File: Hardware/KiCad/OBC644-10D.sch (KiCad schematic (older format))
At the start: 57 parts, among them J1 CONN_11, J2 CONN_11, J3 CONN_4, J4 CONN_6, J5 53047, U1 LT1761ES5-3.3, U10 LT1761ES5-xx, U11 LT1761ES5-xx, U12 M25XX_ROM2, U2 ATMEGA644PA-AUR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

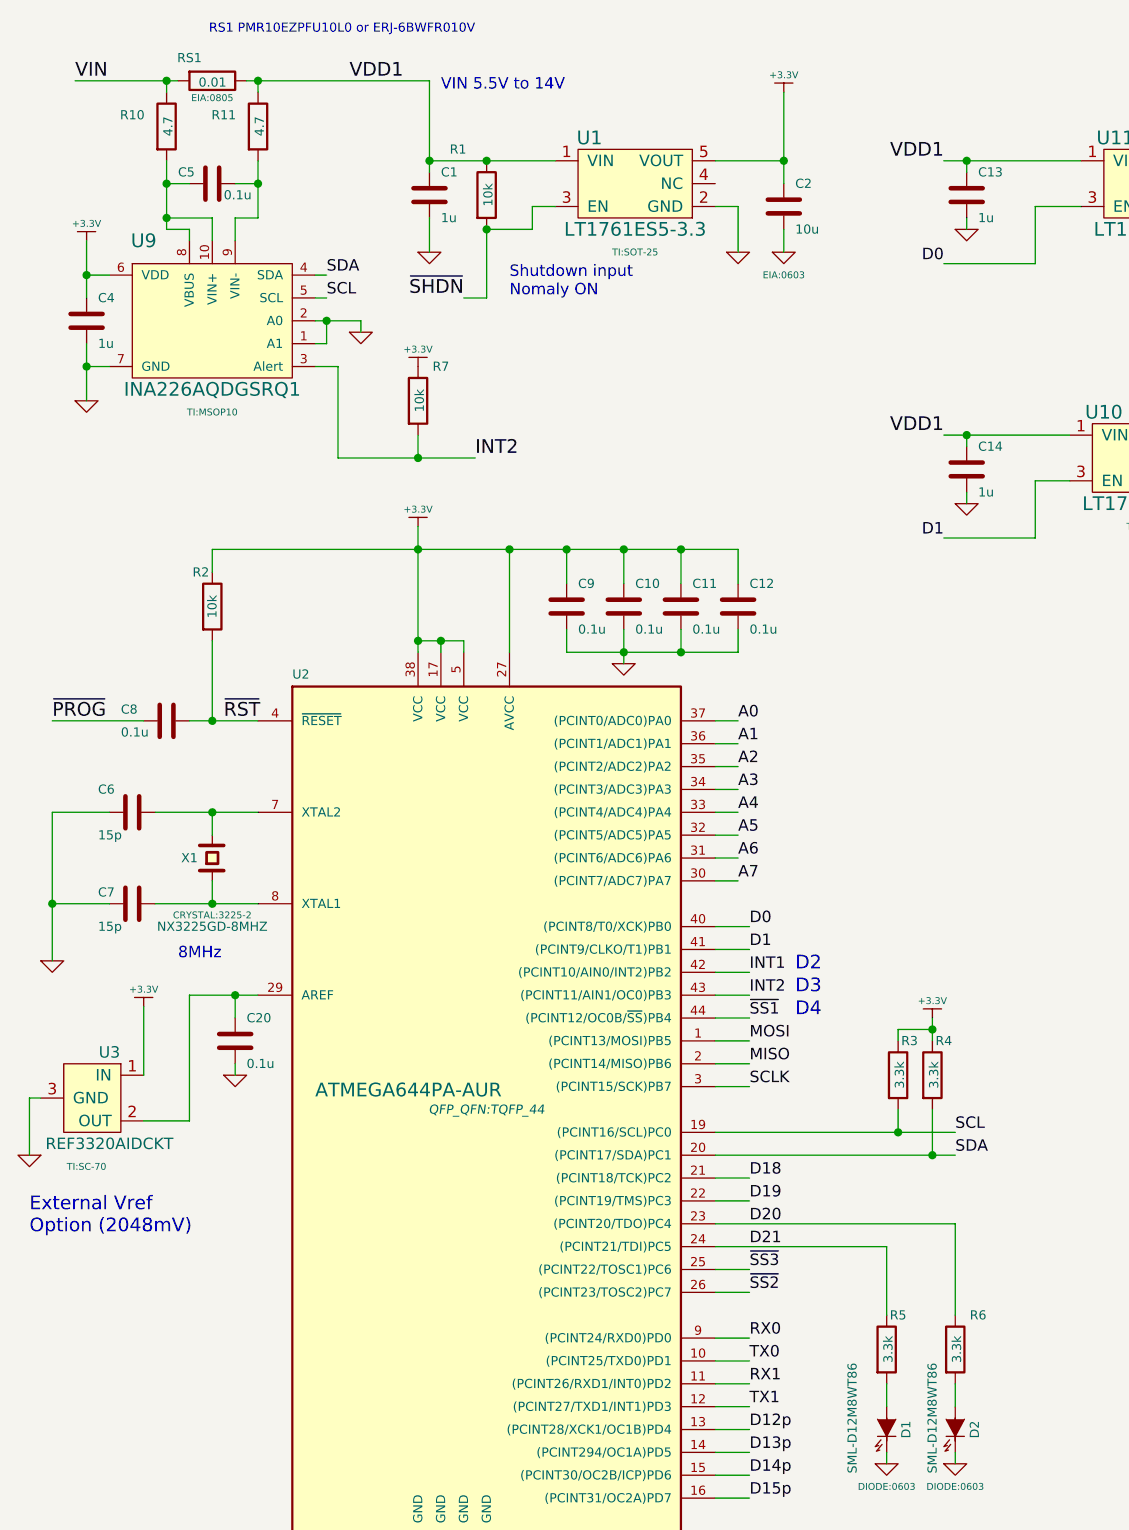
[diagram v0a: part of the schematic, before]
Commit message: Fix PCB and schematic
fix ShuntResistor size & routing
change R5,R6 value
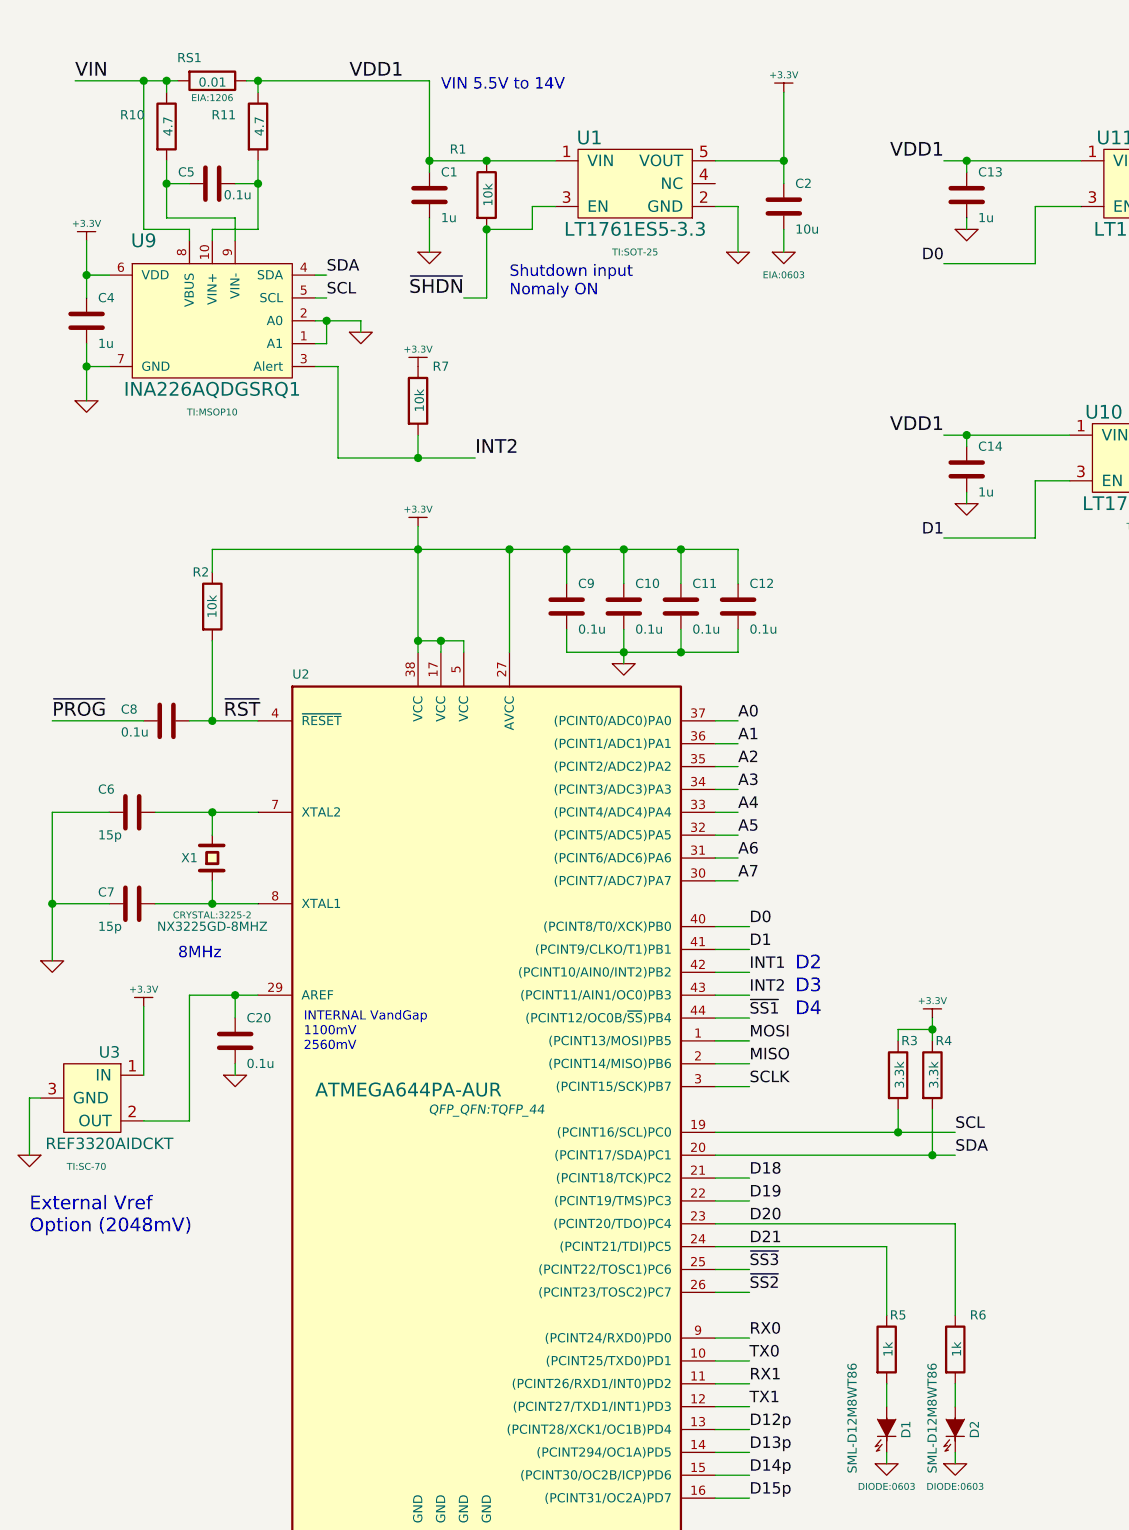
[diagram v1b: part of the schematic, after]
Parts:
- R5, R6: value 3.3k -> 1k
- RS1: footprint EIA:0805 -> EIA:1206
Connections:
- net VIN: now also U9.8 (VBUS)
- net at C5.2, R10.2: now also U9.9 (VIN-); no longer U9.10 (VIN+), U9.8 (VBUS)
- net at C5.1, R11.2: now also U9.10 (VIN+); no longer U9.9 (VIN-)
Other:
- note added: "INTERNAL VandGap\n1100mV\n2560mV"
- note removed: "RS1 PMR10EZPFU10L0 or ERJ-6BWFR010V"
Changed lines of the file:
@@
 LIBS:Sensor
 LIBS:socket
-LIBS:nLog_10DOF-cache
+LIBS:OBC644-10D-cache
 EELAYER 25 0
 EELAYER END
@@
 Sheet 1 1
 Title "OBC1284-10D"
-Date "2017-05-10"
-Rev "C"
+Date "2017-06-03"
+Rev "D"
 Comp "Kent Nakazawa (kent_n@outlook.com) (https://github.com/kentN)"
 Comment1 ""
@@
 P 4750 6300
 F 0 "R6" H 4850 6450 40  0000 C CNN
-F 1 "3.3k" V 4757 6301 40  0000 C CNN
+F 1 "1k" V 4757 6301 40  0000 C CNN
 F 2 "EIA:0402" V 4680 6300 30  0001 C CNN
 F 3 "" H 4750 6300 30  0000 C CNN
@@
 P 4450 6300
 F 0 "R5" H 4500 6450 40  0000 C CNN
-F 1 "3.3k" V 4457 6301 40  0000 C CNN
+F 1 "1k" V 4457 6301 40  0000 C CNN
 F 2 "EIA:0402" V 4380 6300 30  0001 C CNN
 F 3 "" H 4450 6300 30  0000 C CNN
@@
 F 0 "RS1" V 1400 650 40  0000 C CNN
 F 1 "0.01" V 1507 751 40  0000 C CNN
-F 2 "EIA:0805" V 1575 750 30  0000 C CNN
+F 2 "EIA:1206" V 1575 750 30  0000 C CNN
 F 3 "" H 1500 750 30  0000 C CNN
 	1    1500 750
@@
 Wire Wire Line
 	1400 5300 1200 5300
-Wire Wire Line
-	1600 1450 1600 1350
-Wire Wire Line
-	1600 1350 1700 1350
 Connection ~ 1700 750
-Wire Wire Line
-	1300 1350 1500 1350
-Wire Wire Line
-	1500 1350 1500 1450
 Connection ~ 1300 750
 Wire Wire Line
 	1400 1450 1400 1400
-Wire Wire Line
-	1400 1400 1300 1400
-Connection ~ 1300 1350
 Wire Wire Line
 	1050 1600 950  1600
@@
 	1700 750  1700 800
 Wire Wire Line
-	1300 1400 1300 1100
-Wire Wire Line
-	1700 1350 1700 1100
+	1700 1100 1700 1400
 Wire Wire Line
 	1600 1200 1700 1200
@@
 Text Notes 8300 1050 0    60   ~ 0
 Optional SMD ROMs
-Text Notes 2650 550  2    40   ~ 0
-RS1 PMR10EZPFU10L0 or ERJ-6BWFR010V
+Wire Wire Line
+	1300 1350 1300 1100
+Wire Wire Line
+	1400 1400 1200 1400
+Wire Wire Line
+	1200 1400 1200 750
+Connection ~ 1200 750
+Wire Wire Line
+	1300 1350 1600 1350
+Wire Wire Line
+	1600 1350 1600 1450
+Wire Wire Line
+	1700 1400 1500 1400
+Wire Wire Line
+	1500 1400 1500 1450
+Text Notes 1900 5000 0    40   ~ 0
+INTERNAL VandGap\n1100mV\n2560mV
 $EndSCHEMATC

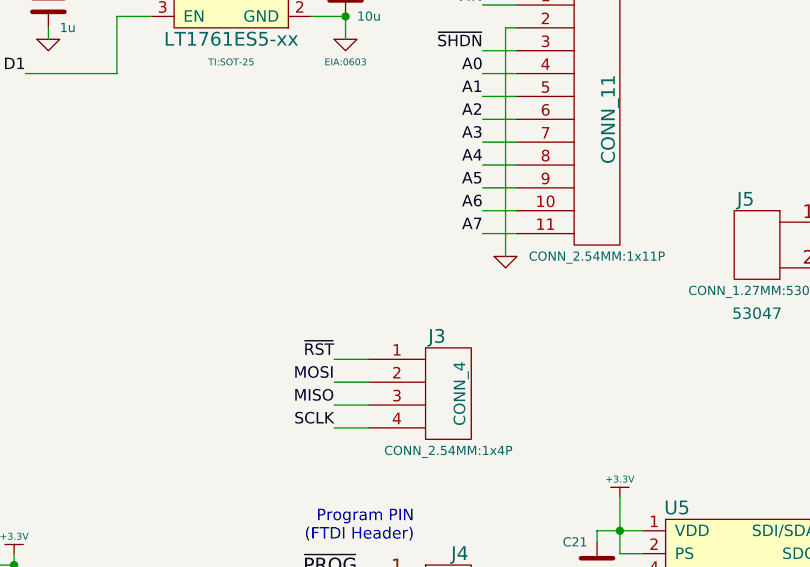
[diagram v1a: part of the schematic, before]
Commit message: Add VCPU OUTPUT
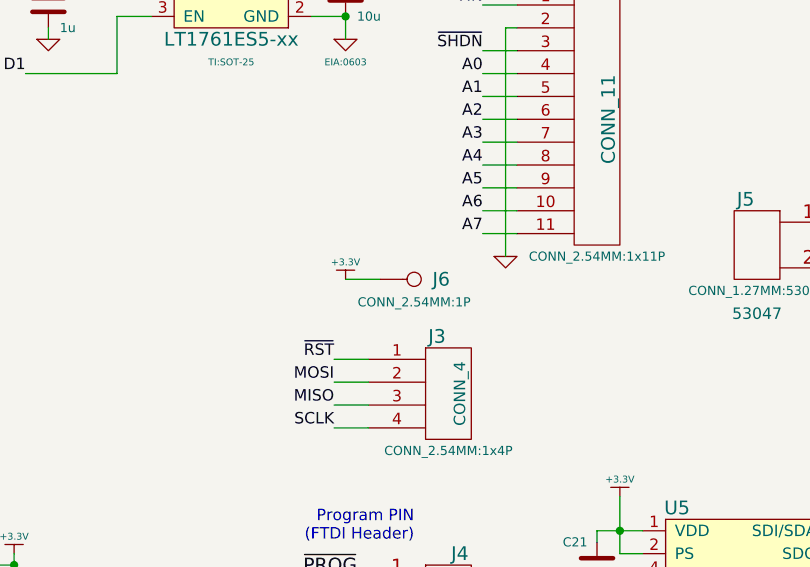
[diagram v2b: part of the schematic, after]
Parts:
- added J6: CONN_1, CONN_2.54MM:1P, symbol CONN_1
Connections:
- net +3.3V: now also J6.1
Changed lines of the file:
@@
 encoding utf-8
 Sheet 1 1
-Title "OBC1284-10D"
-Date "2017-06-03"
-Rev "D"
+Title "OBC644-10D"
+Date "2017-06-04"
+Rev "E"
 Comp "Kent Nakazawa (kent_n@outlook.com) (https://github.com/kentN)"
 Comment1 ""
@@
 Text Notes 1900 5000 0    40   ~ 0
 INTERNAL VandGap\n1100mV\n2560mV
+$Comp
+L CONN_1 J6
+U 1 1 5934CA04
+P 6400 3650
+F 0 "J6" H 6480 3650 60  0000 L CNN
+F 1 "CONN_1" H 6400 3705 30  0001 C CNN
+F 2 "CONN_2.54MM:1P" H 6400 3550 40  0000 C CNN
+F 3 "" H 6400 3650 60  0000 C CNN
+	1    6400 3650
+	1    0    0    -1
+$EndComp
+Wire Wire Line
+	6250 3650 6100 3650
+$Comp
+L +3.3V #PWR047
+U 1 1 5934D1CE
+P 6100 3650
+F 0 "#PWR047" H 6100 3700 10  0001 C CNN
+F 1 "+3.3V" H 6100 3725 30  0000 C CNN
+F 2 "" H 6100 3650 60  0000 C CNN
+F 3 "" H 6100 3650 60  0000 C CNN
+	1    6100 3650
+	1    0    0    -1
+$EndComp
 $EndSCHEMATC

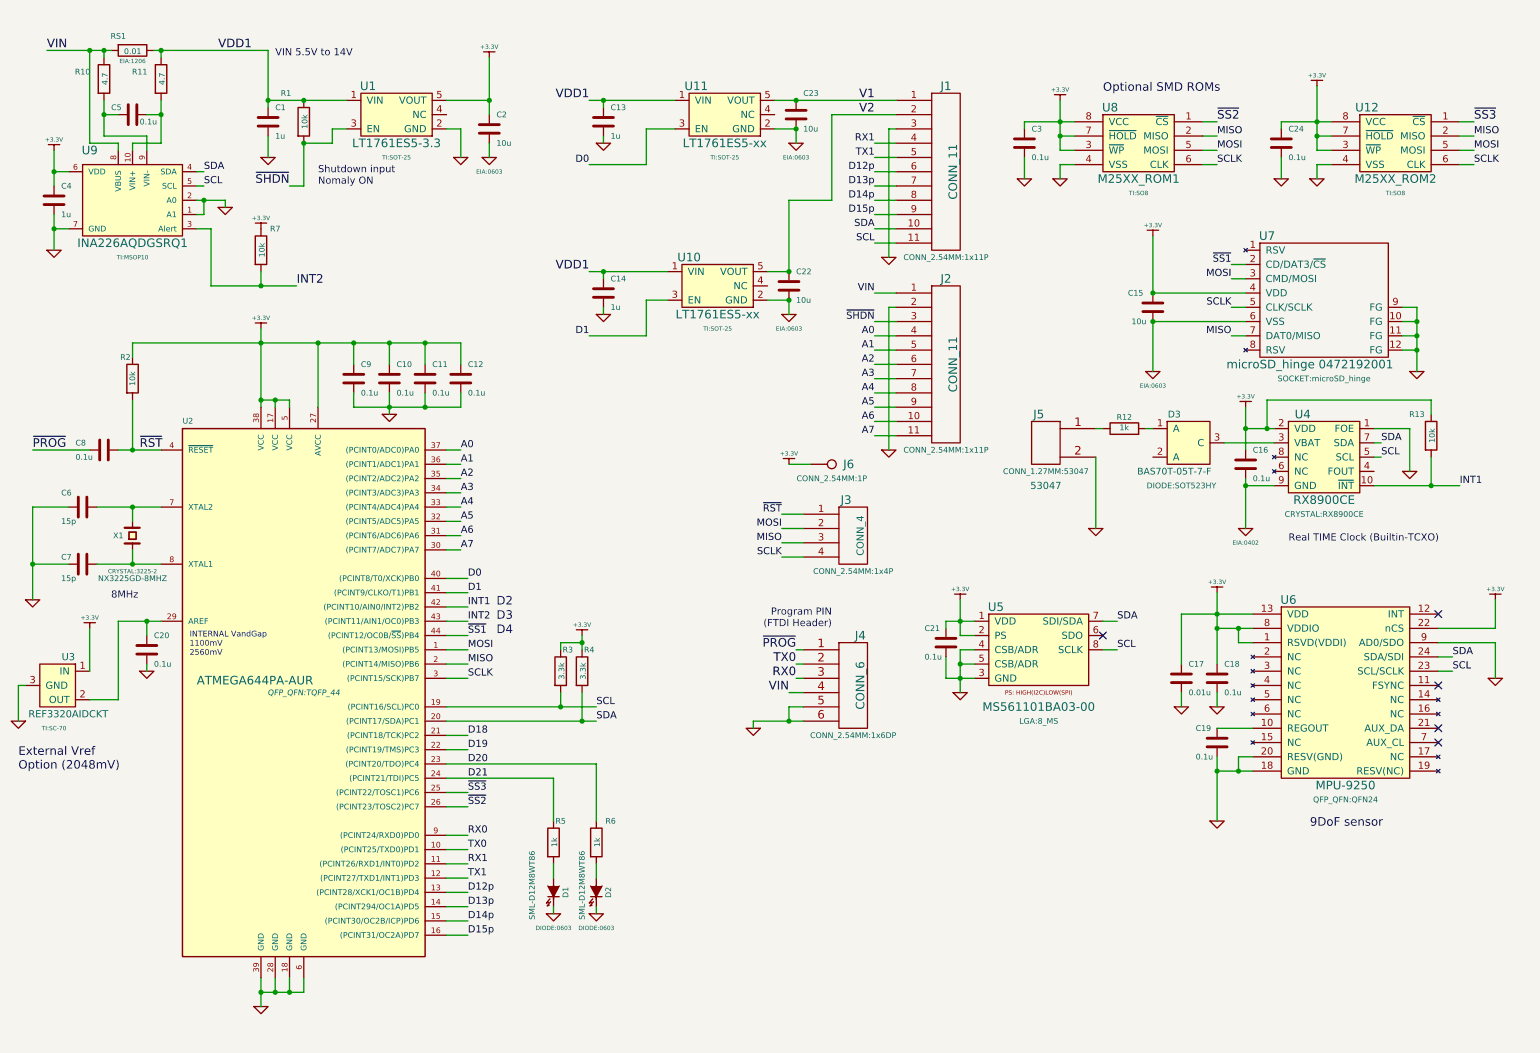
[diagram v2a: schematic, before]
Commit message: Update Rev:E
Add some Pins (3V3, UART_GPIO)
Change SO8-ROM Footprints
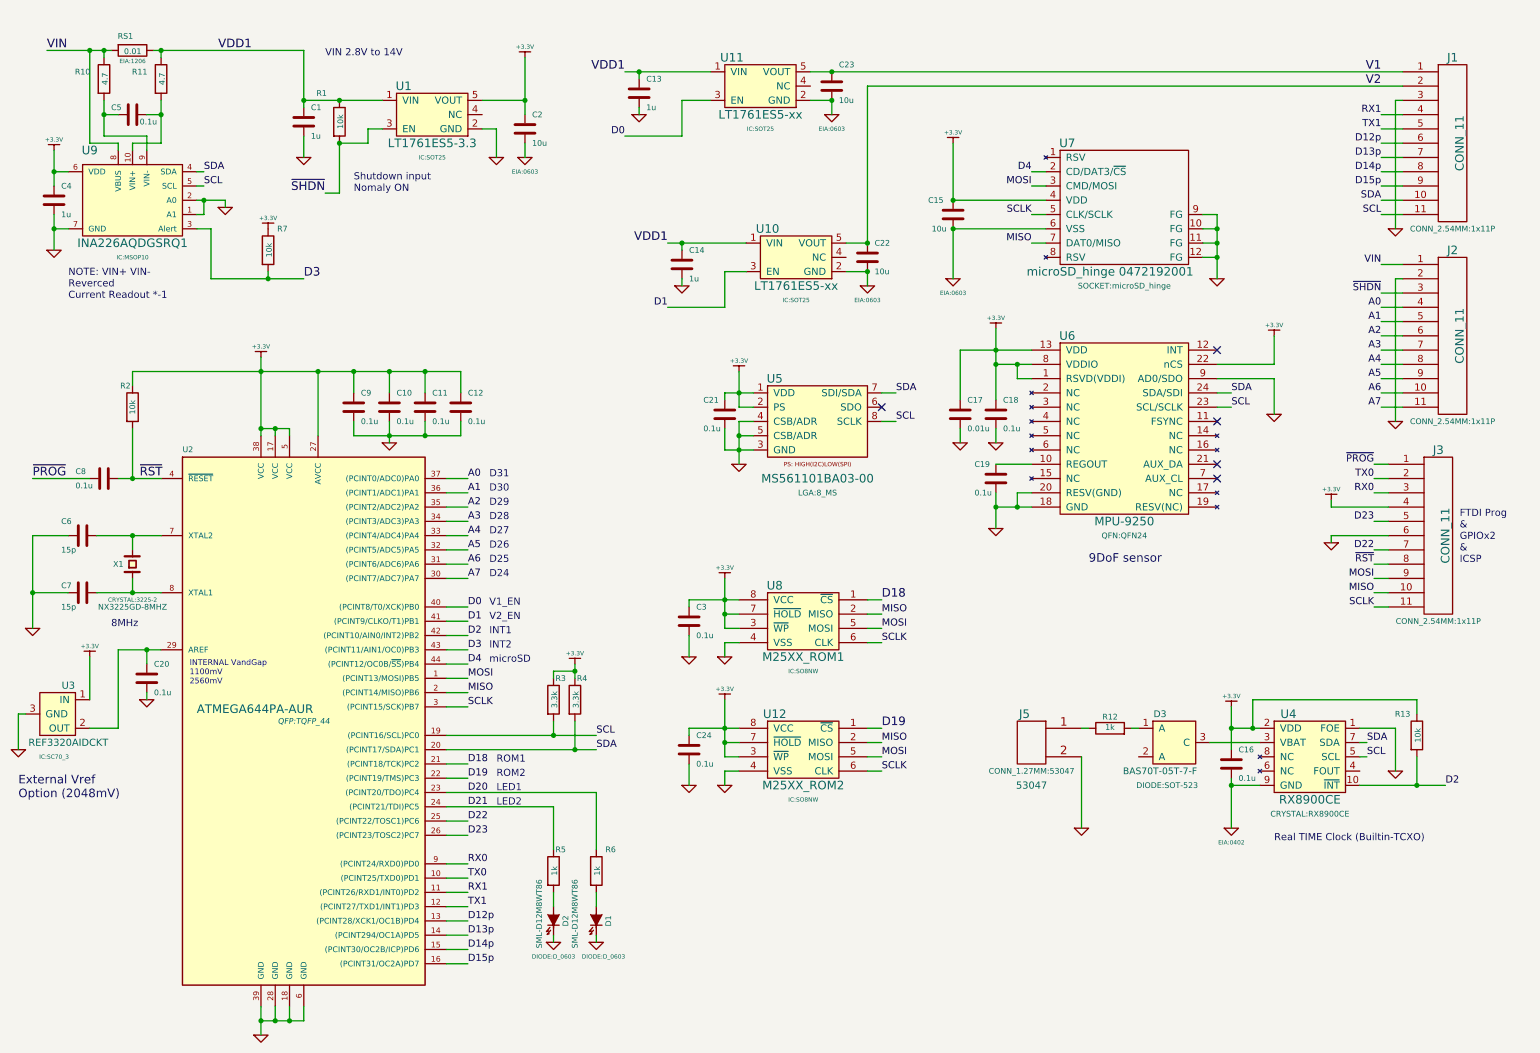
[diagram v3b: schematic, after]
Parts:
- removed J3: CONN_4, CONN_2.54MM:1x4P, symbol CONN_4
- removed J4: CONN_6, CONN_2.54MM:1x6DP, symbol CONN_6
- removed J6: CONN_1, CONN_2.54MM:1P, symbol CONN_1
- added J3: CONN_11, CONN_2.54MM:1x11P, symbol CONN_11
- D1, D2: footprint DIODE:0603 -> DIODE:D_0603
- D3: footprint DIODE:SOT523HY -> DIODE:SOT-523
- U1, U10, U11: footprint TI:SOT-25 -> IC:SOT25
- U12, U8: footprint TI:SO8 -> IC:SO8NW
- U2: footprint QFP_QFN:TQFP_44 -> QFP:TQFP_44
- U3: footprint TI:SC-70 -> IC:SC70_3
- U6: footprint QFP_QFN:QFN24 -> QFN:QFN24
- U9: footprint TI:MSOP10 -> IC:MSOP10
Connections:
- net +3.3V: now also J3.4 (P4)
- net D18: now also U8.1 (~CS~)
- net D19: now also U12.1 (~CS~)
- net GND: now also J3.6 (P6)
- net MISO: now also J3.10 (P10)
- net MOSI: now also J3.9 (P9)
- net RX0: now also J3.3 (P3)
- net SCLK: now also J3.11 (P11)
- net TX0: now also J3.2 (P2)
- net ~PROG: now also J3.1 (P1)
- net ~RST: now also J3.8 (P8)
- net at D2.1 (A): now also R5.2; no longer R6.2
- net at D1.1 (A): now also R6.2; no longer R5.2
- net INT1 renamed D2
- net INT2 renamed D3
- net ~SS1 renamed D4
- net ~SS2 renamed D23
- net D23: now also J3.5 (P5); no longer U8.1 (~CS~)
- net ~SS3 renamed D22
- net D22: now also J3.7 (P7); no longer U12.1 (~CS~)
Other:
- note added: "D24"
- note added: "D25"
- note added: "D26"
- note added: "D27"
- note added: "D28"
- note added: "D29"
- note added: "D30"
- note added: "D31"
- note added: "FTDI Prog\n& \nGPIOx2\n&\nICSP\n"
- note added: "INT1"
- note added: "INT2"
- note added: "LED1"
- note added: "LED2"
- note added: "NOTE: VIN+ VIN-\nReverced\nCurrent Readout *-1"
- note added: "ROM1"
- note added: "ROM2"
- note added: "V1_EN"
- note added: "V2_EN"
- note added: "VIN 2.8V to 14V"
- note added: "microSD"
- note removed: "D2"
- note removed: "D3"
- note removed: "D4"
- note removed: "Optional SMD ROMs"
- note removed: "Program PIN\n(FTDI Header)"
- note removed: "VIN 5.5V to 14V"
- moved on the sheet: C1, C10, C11, C12, C13, C14, C15, C16, C17, C18, C19, C2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
